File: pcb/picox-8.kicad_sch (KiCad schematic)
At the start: 1 part, among them J1 PX-8 Expansion Port

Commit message: some pcb progress
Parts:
- added R1, R10, R12, R19, R20, R21, R22, R23, R24, R31, R32, R33, R34, R35, R36, R4, R43, R44, R45, R46, R47, R48, R55, R56, R57, R58, R59, R6, R60, R8: 1M, Resistor_SMD:R_0603_1608Metric_Pad0.98x0.95mm_HandSolder, symbol Device:R_Small
- added R11, R13, R14, R15, R16, R17, R18, R2, R25, R26, R27, R28, R29, R3, R30, R37, R38, R39, R40, R41, R42, R49, R5, R50, R51, R52, R53, R54, R7, R9: 3.3k, Resistor_SMD:R_0603_1608Metric_Pad0.98x0.95mm_HandSolder, symbol Device:R_Small
- added U1: XC95144XL-TQ100, Package_QFP:TQFP-100_14x14mm_P0.5mm, symbol CPLD_Xilinx:XC95144XL-TQ100
- J1: footprint (none) -> Connector_IDC:IDC-Header_2x25_P2.54mm_Latch_Horizontal
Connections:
- net A12: now reaches J1.1 (A12)
- net A12: now also R25.2
- net A3: now reaches J1.10 (A3)
- net A3: now also R7.2
- net A6: now reaches J1.11 (A6)
- net A6: now also R13.2
- net A5: now reaches J1.12 (A5)
- net A5: now also R11.2
- net A10: now reaches J1.13 (A10)
- net A10: now also R17.2
- net A7: now reaches J1.14 (A7)
- net A7: now also R14.2
- net A8: now reaches J1.15 (A8)
- net A8: now also R15.2
- net A9: now reaches J1.16 (A9)
- net A9: now also R16.2
- net D0: now reaches J1.17 (D0)
- net D0: now also R29.2
- net D1: now reaches J1.18 (D1)
- net D1: now also R30.2
- net D2: now reaches J1.19 (D2)
- net D2: now also R37.2
- net A11: now reaches J1.2 (A11)
- net A11: now also R18.2, R53.2, R54.2
- net D3: now reaches J1.20 (D3)
- net D3: now also R38.2
- net D4: now reaches J1.21 (D4)
- net D4: now also R39.2
- net D5: now reaches J1.22 (D5)
- net D5: now also R40.2
- net D6: now reaches J1.23 (D6)
- net D6: now also R41.2
- net D7: now reaches J1.24 (D7)
- net D7: now also R42.2
- net ~{BUSRQ}: now reaches J1.25 (~{BUSRQ})
- net ~{BUSAK}: now reaches J1.26 (~{BUSAK})
- net ~{M1}: now reaches J1.27 (~{M1})
- net ~{WAIT}: now reaches J1.28 (~{WAIT})
- net VL: now reaches J1.29 (VL)
- net A14: now reaches J1.3 (A13)
- net A14: now also R27.2
- net ~{HLTA}: now reaches J1.30 (~{HLTA})
- net GND: now reaches J1.31 (GND)
- net GND: now also J1.32 (GND), R1.2, R10.2, R12.2, R19.2, R20.2, R21.2, R22.2, R23.2, R24.2, R31.2, R32.2, R33.2, R34.2, R35.2, R36.2, R4.2, R43.2, R44.2, R45.2, R46.2, R47.2, R48.2, R55.2, R56.2, R57.2, R58.2, R59.2, R6.2, R60.2, R8.2
- net ~{RS}: now reaches J1.33 (~{RESET})
- net SPI: now reaches J1.34 (SPI)
- net ~{RD}: now reaches J1.35 (~{RD})
- net ~{RD}: now also R50.2
- net ~{MREQ}: now reaches J1.36 (~{MREQ})
- net ~{MREQ}: now also R52.2
- net ~{WR}: now reaches J1.37 (~{WR})
- net ~{WR}: now also R49.2
- net ~{CLK}: now reaches J1.38 (~{CLK})
- net VCH: now reaches J1.39 (VCH)
- net A13: now reaches J1.4 (A13)
- net A13: now also R26.2
- net ~{IORQ}: now reaches J1.40 (~{IORQ})
- net ~{IORQ}: now also R51.2
- net DCAS: now reaches J1.41 (DCAS)
- net DW: now reaches J1.42 (DW)
- net ~{INTEX}: now reaches J1.43 (~{INTEX})
- net OFF: now reaches J1.44 (OFF)
- net ~{RXD}: now reaches J1.45 (~{RXD})
- net ~{TXD}: now reaches J1.46 (~{TXD})
- net VB1: now reaches J1.47 (VB1)
- net ~{BK2}: now reaches J1.48 (~{BK2})
- net CG: now reaches J1.49 (CG)
- net CG: now also J1.50 (CG)
- net A1: now reaches J1.5 (A1)
- net A1: now also R3.2
- net A2: now reaches J1.6 (A2)
- net A2: now also R5.2
- net A15: now reaches J1.7 (A15)
- net A15: now also R28.2
- net A0: now reaches J1.8 (A0)
- net A0: now also R2.2
- net A4: now reaches J1.9 (A4)
- net A4: now also R9.2
- new net BA0: R1.1, R2.1, U1.79 (P79)
- new net BA1: R3.1, R4.1
- new net BA10: R17.1, R23.1
- new net BA11: R18.1, R24.1, R53.1, R54.1, R59.1, R60.1, U1.76 (P76)
- new net BA12: R25.1, R31.1
- new net BA13: R26.1, R32.1, U1.77 (P77)
- new net BA14: R27.1, R33.1
- new net BA15: R28.1, R34.1
- new net BA2: R5.1, R6.1, U1.78 (P78)
- new net BA3: R7.1, R8.1, U1.80 (P80)
- new net BA4: R10.1, R9.1
- new net BA5: R11.1, R12.1, U1.81 (P81)
- new net BA6: R13.1, R19.1
- new net BA7: R14.1, R20.1
- new net BA8: R15.1, R21.1
- new net BA9: R16.1, R22.1
- new net BD0: R29.1, R35.1
- new net BD1: R30.1, R36.1
- new net BD2: R37.1, R43.1
- new net BD3: R38.1, R44.1
- new net BD4: R39.1, R45.1
- new net BD5: R40.1, R46.1
- new net BD6: R41.1, R47.1
- new net BD7: R42.1, R48.1
- new net B~{IORQ}: R51.1, R57.1
- new net B~{MREQ}: R52.1, R58.1
- new net B~{RD}: R50.1, R56.1
- new net B~{WR}: R49.1, R55.1
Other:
- moved on the sheet: J1

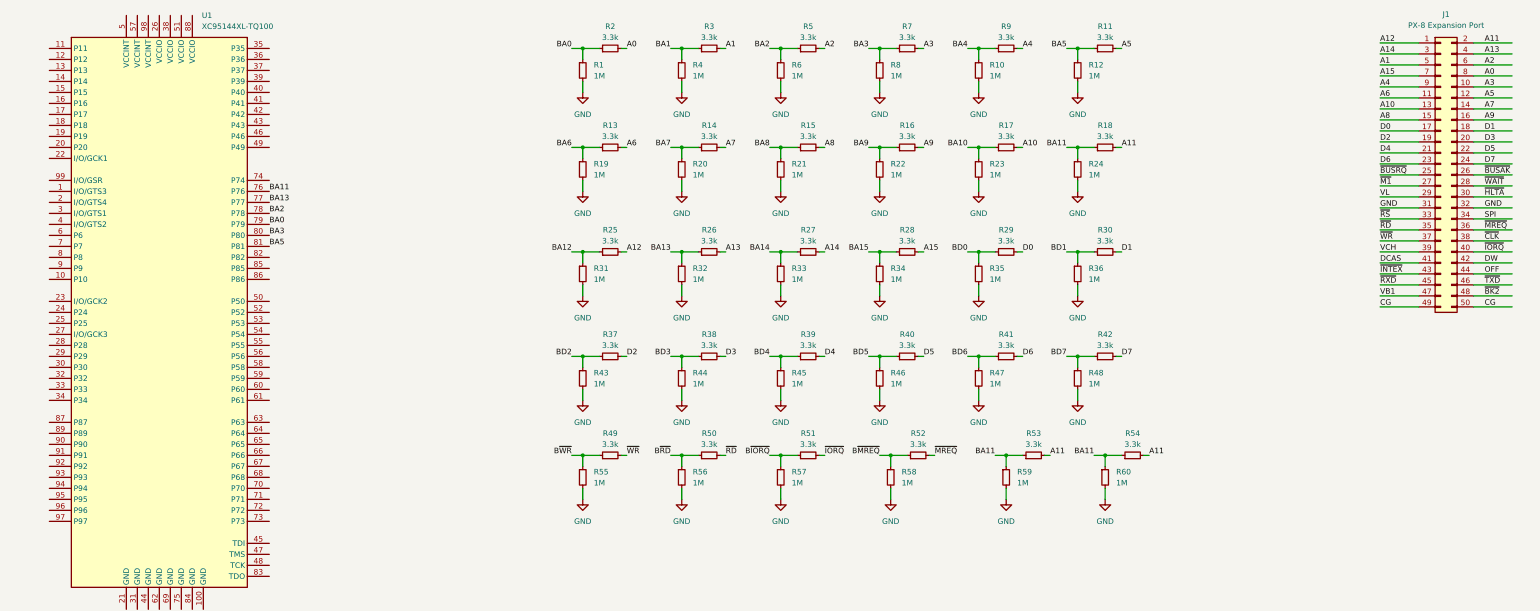
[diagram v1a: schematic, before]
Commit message: add bus current limiting and pull resistors
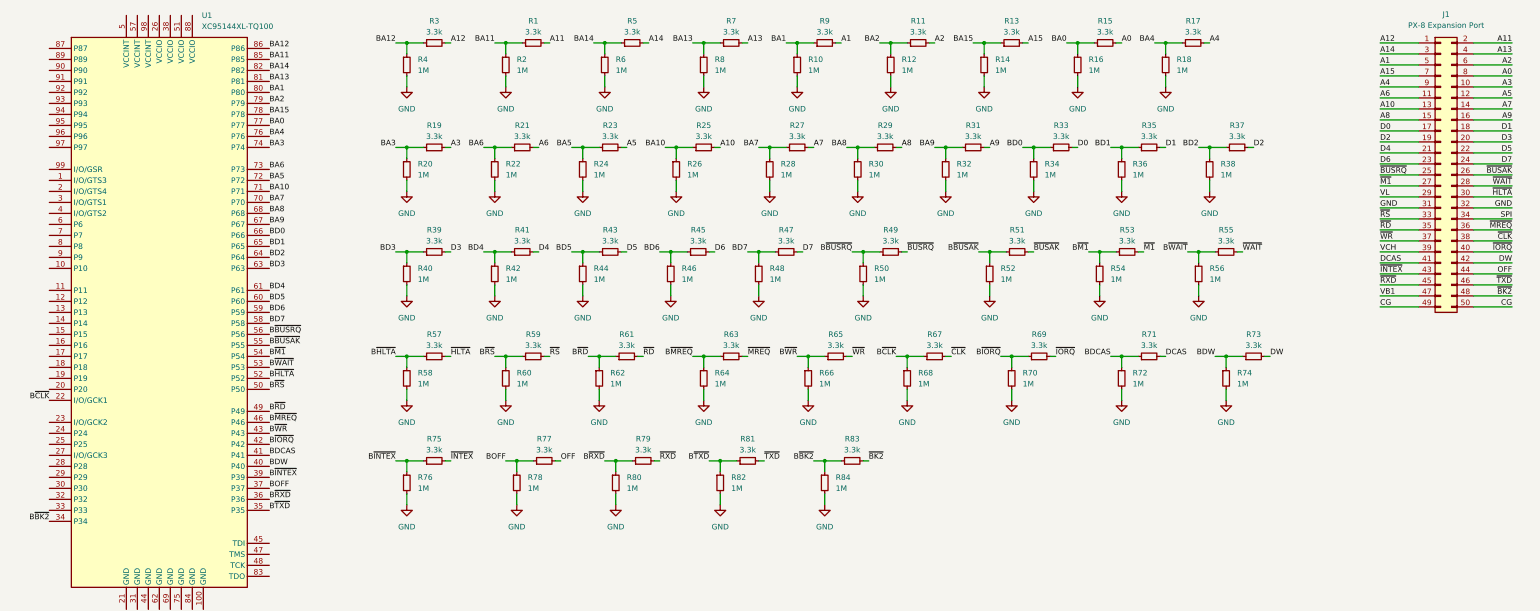
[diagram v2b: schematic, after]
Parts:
- added R61, R63, R65, R67, R69, R71, R73, R75, R77, R79, R81, R83: 3.3k, Resistor_SMD:R_0603_1608Metric_Pad0.98x0.95mm_HandSolder, symbol Device:R_Small
- added R62, R64, R66, R68, R70, R72, R74, R76, R78, R80, R82, R84: 1M, Resistor_SMD:R_0603_1608Metric_Pad0.98x0.95mm_HandSolder, symbol Device:R_Small
- R1, R19, R21, R23, R31, R33, R35, R43, R45, R47, R55, R57, R59: value 1M -> 3.3k
- R14, R16, R18, R2, R26, R28, R30, R38, R40, R42, R50, R52, R54: value 3.3k -> 1M
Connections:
- net A0: now also R15.2; no longer R2.2
- net A1: now also R9.2; no longer R3.2
- net A10: now also R25.2; no longer R17.2
- net A11: now also R1.2; no longer R18.2, R53.2, R54.2
- net A12: now also R3.2; no longer R25.2
- net A13: now also R7.2; no longer R26.2
- net A14: now also R5.2; no longer R27.2
- net A15: now also R13.2; no longer R28.2
- net A2: now also R11.2; no longer R5.2
- net A3: now also R19.2; no longer R7.2
- net A4: now also R17.2; no longer R9.2
- net A5: now also R23.2; no longer R11.2
- net A6: now also R21.2; no longer R13.2
- net A7: now also R27.2; no longer R14.2
- net A8: now also R29.2; no longer R15.2
- net A9: now also R31.2; no longer R16.2
- net BA0: now also R15.1, R16.1, U1.77 (P77); no longer R1.1, R2.1, U1.79 (P79)
- net BA1: now also R10.1, R9.1, U1.80 (P80); no longer R3.1, R4.1
- net BA10: now also R25.1, R26.1, U1.71 (P71); no longer R17.1, R23.1
- net BA11: now also R1.1, R2.1, U1.85 (P85); no longer R18.1, R24.1, R53.1, R54.1, R59.1, R60.1, U1.76 (P76)
- net BA12: now also R3.1, R4.1, U1.86 (P86); no longer R25.1, R31.1
- net BA13: now also R7.1, R8.1, U1.81 (P81); no longer R26.1, R32.1, U1.77 (P77)
- net BA14: now also R5.1, R6.1, U1.82 (P82); no longer R27.1, R33.1
- net BA15: now also R13.1, R14.1, U1.78 (P78); no longer R28.1, R34.1
- net BA2: now also R11.1, R12.1, U1.79 (P79); no longer R5.1, R6.1, U1.78 (P78)
- net BA3: now also R19.1, R20.1, U1.74 (P74); no longer R7.1, R8.1, U1.80 (P80)
- net BA4: now also R17.1, R18.1, U1.76 (P76); no longer R10.1, R9.1
- net BA5: now also R23.1, R24.1, U1.72 (P72); no longer R11.1, R12.1, U1.81 (P81)
- net BA6: now also R21.1, R22.1, U1.73 (P73); no longer R13.1, R19.1
- net BA7: now also R27.1, R28.1, U1.70 (P70); no longer R14.1, R20.1
- net BA8: now also R29.1, R30.1, U1.68 (P68); no longer R15.1, R21.1
- net BA9: now also R31.1, R32.1, U1.67 (P67); no longer R16.1, R22.1
- net BD0: now also R33.1, R34.1, U1.66 (P66); no longer R29.1, R35.1
- net BD1: now also R35.1, U1.65 (P65); no longer R30.1
- net BD2: now also R38.1, U1.64 (P64); no longer R43.1
- net BD3: now also R39.1, R40.1, U1.63 (P63); no longer R38.1, R44.1
- net BD4: now also R41.1, R42.1, U1.61 (P61); no longer R39.1, R45.1
- net BD5: now also R43.1, R44.1, U1.60 (P60); no longer R40.1, R46.1
- net BD6: now also R45.1, R46.1, U1.59 (P59); no longer R41.1, R47.1
- net BD7: now also R47.1, U1.58 (P58); no longer R42.1
- net B~{IORQ}: now also U1.42 (P42), R69.1, R70.1; no longer R51.1, R57.1
- net B~{MREQ}: now also U1.46 (P46), R63.1, R64.1; no longer R52.1, R58.1
- net B~{RD}: now also U1.49 (P49), R61.1, R62.1; no longer R50.1, R56.1
- net B~{WR}: now also U1.43 (P43), R65.1, R66.1; no longer R49.1, R55.1
- net D0: now also R33.2; no longer R29.2
- net D1: now also R35.2; no longer R30.2
- net D3: now also R39.2; no longer R38.2
- net D4: now also R41.2; no longer R39.2
- net D5: now also R43.2; no longer R40.2
- net D6: now also R45.2; no longer R41.2
- net D7: now also R47.2; no longer R42.2
- net DCAS: now also R71.2
- net DW: now also R73.2
- net GND: now also R14.2, R16.2, R18.2, R2.2, R26.2, R28.2, R30.2, R38.2, R40.2, R42.2, R50.2, R52.2, R54.2, R62.2, R64.2, R66.2, R68.2, R70.2, R72.2, R74.2, R76.2, R78.2, R80.2, R82.2, R84.2; no longer R1.2, R19.2, R21.2, R23.2, R31.2, R33.2, R35.2, R43.2, R45.2, R47.2, R55.2, R57.2, R59.2
- net OFF: now also R77.2
- net ~{BK2}: now also R83.2
- net ~{BUSAK}: now also R51.2
- net ~{BUSRQ}: now also R49.2
- net ~{CLK}: now also R67.2
- net ~{HLTA}: now also R57.2
- net ~{INTEX}: now also R75.2
- net ~{IORQ}: now also R69.2; no longer R51.2
- net ~{M1}: now also R53.2
- net ~{MREQ}: now also R63.2; no longer R52.2
- net ~{RD}: now also R61.2; no longer R50.2
- net ~{RS}: now also R59.2
- net ~{RXD}: now also R79.2
- net ~{TXD}: now also R81.2
- net ~{WAIT}: now also R55.2
- net ~{WR}: now also R65.2; no longer R49.2
- net B~{CLK}: now reaches U1.22 (I/O/GCK1)
- net B~{CLK}: now also R67.1, R68.1
- net B~{BK2}: now reaches U1.34 (P34)
- net B~{BK2}: now also R83.1, R84.1
- net B~{TXD}: now reaches U1.35 (P35)
- net B~{TXD}: now also R81.1, R82.1
- net B~{RXD}: now reaches U1.36 (P36)
- net B~{RXD}: now also R79.1, R80.1
- net BOFF: now reaches U1.37 (P37)
- net BOFF: now also R77.1, R78.1
- net B~{INTEX}: now reaches U1.39 (P39)
- net B~{INTEX}: now also R75.1, R76.1
- net BDW: now reaches U1.40 (P40)
- net BDW: now also R73.1, R74.1
- net BDCAS: now reaches U1.41 (P41)
- net BDCAS: now also R71.1, R72.1
- net B~{RS}: now reaches U1.50 (P50)
- net B~{RS}: now also R59.1, R60.1
- net B~{HLTA}: now reaches U1.52 (P52)
- net B~{HLTA}: now also R57.1, R58.1
- net B~{WAIT}: now reaches U1.53 (P53)
- net B~{WAIT}: now also R55.1, R56.1
- net B~{M1}: now reaches U1.54 (P54)
- net B~{M1}: now also R53.1, R54.1
- net B~{BUSAK}: now reaches U1.55 (P55)
- net B~{BUSAK}: now also R51.1, R52.1
- net B~{BUSRQ}: now reaches U1.56 (P56)
- net B~{BUSRQ}: now also R49.1, R50.1

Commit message: PCB work
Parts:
- added J2: Mini-DIN-8, Connector_DIN:minidin-8, symbol Connector:Mini-DIN-8
- added J3: SD_Card, Connector_Card:SD_TE_2041021, symbol Connector:SD_Card
- added SW1: SW_Push, Button_Switch_THT:SW_Tactile_SPST_Angled_PTS645Vx39-2LFS, symbol Switch:SW_Push
- added U2: MAX3232, Package_SO:SOP-16_3.9x9.9mm_P1.27mm, symbol Interface_UART:MAX3232
- added U3: Pico_W, RPI PIco:RPi_Pico_SMD_TH, symbol MCU_RaspberryPi_and_Boards:Pico_W
- added U4: AZ1117-3.3, Package_TO_SOT_SMD:SOT-223, symbol Regulator_Linear:AZ1117-3.3
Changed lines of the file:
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@@
+    )
+  )
+  (symbol (lib_id "Connector:Mini-DIN-8") (at 41.91 340.36 0) (unit 1)
+    (in_bom yes) (on_board yes) (dnp no) (fields_autoplaced)
+    (property "Reference" "J2" (at 43.5611 330.2 0)
+      (effects (font (size 1.27 1.27)) (justify left))
+    )
+    (property "Value" "Mini-DIN-8" (at 43.5611 332.74 0)
+      (effects (font (size 1.27 1.27)) (justify left))
+    )
+    (property "Footprint" "Connector_DIN:minidin-8" (at 41.656 340.614 90)
+      (effects (font (size 1.27 1.27)) hide)
+    )
+    (property "Datasheet" "http://service.powerdynamics.com/ec/Catalog17/Section%2011.pdf" (at 41.656 340.614 90)
+      (effects (font (size 1.27 1.27)) hide)
+    )
+    (pin "1")
+    (pin "2")
+    (pin "3")
+    (pin "4")
+    (pin "5")
+    (pin "6")
+    (pin "7")
+    (pin "8")
+    (instances
+      (project "picox-8"
+        (path "/b3edc386-2a93-4110-82fb-ef41abb72a44"
+          (reference "J2") (unit 1)
+        )
+      )
     )
   )
@@
     )
   )
+  (symbol (lib_id "Switch:SW_Push") (at 468.63 111.76 0) (unit 1)
+    (in_bom yes) (on_board yes) (dnp no) (fields_autoplaced)
+    (property "Reference" "SW1" (at 468.63 104.14 0)
+      (effects (font (size 1.27 1.27)))
+    )
+    (property "Value" "SW_Push" (at 468.63 106.68 0)
+      (effects (font (size 1.27 1.27)))
+    )
+    (property "Footprint" "Button_Switch_THT:SW_Tactile_SPST_Angled_PTS645Vx39-2LFS" (at 468.63 106.68 0)
+      (effects (font (size 1.27 1.27)) hide)
+    )
+    (property "Datasheet" "~" (at 468.63 106.68 0)
+      (effects (font (size 1.27 1.27)) hide)
+    )
+    (pin "1")
+    (pin "2")
+    (instances
+      (project "picox-8"
+        (path "/b3edc386-2a93-4110-82fb-ef41abb72a44"
+          (reference "SW1") (unit 1)
+        )
+      )
+    )
+  )
   (symbol (lib_id "Device:R_Small") (at 298.45 74.93 90) (unit 1)
     (in_bom yes) (on_board yes) (dnp no) (fields_autoplaced)
@@
     )
   )
+  (symbol (lib_id "Connector:SD_Card") (at 106.68 316.23 0) (unit 1)
+    (in_bom yes) (on_board yes) (dnp no) (fields_autoplaced)
+    (property "Reference" "J3" (at 106.68 298.45 0)
+      (effects (font (size 1.27 1.27)))
+    )
+    (property "Value" "SD_Card" (at 106.68 300.99 0)
+      (effects (font (size 1.27 1.27)))
+    )
+    (property "Footprint" "Connector_Card:SD_TE_2041021" (at 106.68 316.23 0)
+      (effects (font (size 1.27 1.27)) hide)
+    )
+    (property "Datasheet" "http://portal.fciconnect.com/Comergent//fci/drawing/10067847.pdf" (at 106.68 316.23 0)
+      (effects (font (size 1.27 1.27)) hide)
+    )
+    (pin "1")
+    (pin "10")
+    (pin "11")
+    (pin "12")
+    (pin "13")
+    (pin "2")
+    (pin "3")
+    (pin "4")
+    (pin "5")
+    (pin "6")
+    (pin "7")
+    (pin "8")
+    (pin "9")
+    (instances
+      (project "picox-8"
+        (path "/b3edc386-2a93-4110-82fb-ef41abb72a44"
+          (reference "J3") (unit 1)
+        )
+      )
+    )
+  )
   (symbol (lib_id "Device:R_Small") (at 135.89 74.93 90) (unit 1)
     (in_bom yes) (on_board yes) (dnp no) (fields_autoplaced)
@@
     )
   )
+  (symbol (lib_id "MCU_RaspberryPi_and_Boards:Pico_W") (at 346.71 215.9 0) (unit 1)
+    (in_bom yes) (on_board yes) (dnp no) (fields_autoplaced)
+    (property "Reference" "U3" (at 346.71 184.15 0)
+      (effects (font (size 1.27 1.27)))
+    )
+    (property "Value" "Pico_W" (at 346.71 186.69 0)
+      (effects (font (size 1.27 1.27)))
+    )
+    (property "Footprint" "RPI PIco:RPi_Pico_SMD_TH" (at 346.71 215.9 90)
+      (effects (font (size 1.27 1.27)) hide)
+    )
+    (property "Datasheet" "" (at 346.71 215.9 0)
+      (effects (font (size 1.27 1.27)) hide)
+    )
+    (pin "1")
+    (pin "10")
+    (pin "11")
+    (pin "12")
+    (pin "13")
+    (pin "14")
+    (pin "15")
+    (pin "16")
+    (pin "17")
+    (pin "18")
+    (pin "19")
+    (pin "2")
+    (pin "20")
+    (pin "21")
+    (pin "22")
+    (pin "23")
+    (pin "24")
+    (pin "25")
+    (pin "26")
+    (pin "27")
+    (pin "28")
+    (pin "29")
+    (pin "3")
+    (pin "30")
+    (pin "31")
+    (pin "32")
+    (pin "33")
+    (pin "34")
+    (pin "35")
+    (pin "36")
+    (pin "37")
+    (pin "38")
+    (pin "39")
+    (pin "4")
+    (pin "40")
+    (pin "5")
+    (pin "6")
+    (pin "7")
+    (pin "8")
+    (pin "9")
+    (instances
+      (project "picox-8"
+        (path "/b3edc386-2a93-4110-82fb-ef41abb72a44"
+          (reference "U3") (unit 1)
+        )
+      )
+    )
+  )
   (symbol (lib_id "power:GND") (at 109.22 85.09 0) (unit 1)
     (in_bom yes) (on_board yes) (dnp no) (fields_autoplaced)
@@
         (path "/b3edc386-2a93-4110-82fb-ef41abb72a44"
           (reference "R25") (unit 1)
+        )
+      )
+    )
+  )
+  (symbol (lib_id "Interface_UART:MAX3232") (at 68.58 226.06 0) (unit 1)
+    (in_bom yes) (on_board yes) (dnp no) (fields_autoplaced)
+    (property "Reference" "U2" (at 70.7741 195.58 0)
+      (effects (font (size 1.27 1.27)) (justify left))
+    )
+    (property "Value" "MAX3232" (at 70.7741 198.12 0)
+      (effects (font (size 1.27 1.27)) (justify left))
+    )
+    (property "Footprint" "Package_SO:SOP-16_3.9x9.9mm_P1.27mm" (at 69.85 252.73 0)
+      (effects (font (size 1.27 1.27)) (justify left) hide)
+    )
+    (property "Datasheet" "https://datasheets.maximintegrated.com/en/ds/MAX3222-MAX3241.pdf" (at 68.58 223.52 0)
+      (effects (font (size 1.27 1.27)) hide)
+    )
+    (pin "1")
+    (pin "10")
+    (pin "11")
+    (pin "12")
+    (pin "13")
+    (pin "14")
+    (pin "15")
+    (pin "16")
+    (pin "2")
+    (pin "3")
+    (pin "4")
+    (pin "5")
+    (pin "6")
+    (pin "7")
+    (pin "8")
+    (pin "9")
+    (instances
+      (project "picox-8"
+        (path "/b3edc386-2a93-4110-82fb-ef41abb72a44"
+          (reference "U2") (unit 1)
         )
       )
@@
         )
       )
+    )
+  )
+  (symbol (lib_id "Regulator_Linear:AZ1117-3.3") (at 166.37 185.42 0) (unit 1)
+    (in_bom yes) (on_board yes) (dnp no) (fields_autoplaced)
+    (property "Reference" "U4" (at 166.37 179.07 0)
+      (effects (font (size 1.27 1.27)))
+    )
+    (property "Value" "AZ1117-3.3" (at 166.37 181.61 0)
+      (effects (font (size 1.27 1.27)))
+    )
+    (property "Footprint" "Package_TO_SOT_SMD:SOT-223" (at 166.37 179.07 0)
+      (effects (font (size 1.27 1.27) italic) hide)
+    )
+    (property "Datasheet" "https://www.diodes.com/assets/Datasheets/AZ1117.pdf" (at 166.37 185.42 0)
+      (effects (font (size 1.27 1.27)) hide)
+    )
+    (pin "1")
+    (pin "2")
+    (pin "3")
+    (instances
+      (project "picox-8"
+        (path "/b3edc386-2a93-4110-82fb-ef41abb72a44"
+          (reference "U4") (unit 1)
+        )
+      )
